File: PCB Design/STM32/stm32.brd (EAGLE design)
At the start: 71.1 x 45.7 mm, 68 parts, among them IC1 NCP1117ST50T3G, Q1 8MHz, T1 SFH303, T2 SFH303, T3 SFH303, T4 SFH303, U1 STM32F103RET6, U2 MCP1700T-3302E/TT, U3 MCP1700T-3302E/TT, U4 MPU-6050, U5 TB6612FNG, X1 22-23-2031

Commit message: update8
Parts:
- moved C15 1.80 mm to (72.1, 34.9)
- moved C19 1.44 mm to (67.6, 34.9), turned to 180 degrees
- moved R9 1.27 mm to (88.9, 72.6), turned to 90 degrees
- moved R8 0.92 mm to (83.8, 72.6), turned to 90 degrees
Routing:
- net 5V: track 61.6 -> 132.7 mm, vias 1 -> 0
- net V_BATT: track 23.4 -> 73.3 mm
- net VCC: track 169.4 -> 135.2 mm
- net IR_OUT3: track 23.5 -> 0.00 mm, vias 2 -> 0
- net USART1_RX: track 14.2 -> 0.00 mm
- net GND: track 183.0 -> 194.6 mm, vias 9 -> 10
- net IR_IN3: track 14.0 -> 23.2 mm
- net IR_IN2: track 0.00 -> 9.24 mm
- net JTAG-TCK: track 6.50 -> 2.64 mm
- net JTAG-TDO: track 11.5 -> 9.16 mm
- net JTAG-TMS: track 9.83 -> 7.67 mm
- net M2-: track 43.4 -> 42.5 mm, vias 1 -> 2
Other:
- outline, holes or cut-outs redrawn

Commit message: meal save
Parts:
- moved U$1 1.02 mm to (97.8, 56.1)
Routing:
- net VCC: track 135.2 -> 67.7 mm
- net M2CB: track 32.7 -> 0.00 mm
- net M2CA: track 26.0 -> 0.00 mm
- net USART1_TX: track 15.5 -> 0.00 mm, vias 1 -> 0
- net GND: track 194.6 -> 179.3 mm, vias 10 -> 15
- net RST: track 14.8 -> 0.00 mm
- net LED3: track 0.00 -> 14.0 mm
- net IR_IN3: track 23.2 -> 9.24 mm, vias 1 -> 0
- net IR_IN4: track 12.8 -> 0.00 mm, vias 1 -> 0
- net N$14: track 0.00 -> 10.2 mm
- net JTAG-TDO: track 9.16 -> 0.06 mm
- net N$7: track 0.00 -> 7.84 mm, vias 0 -> 1
- net JTAG-TMS: track 7.67 -> 0.06 mm
- net N$5: track 0.00 -> 5.85 mm, vias 0 -> 1
- net JTAG-TCK: track 2.64 -> 0.00 mm
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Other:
- board size 71.1 x 45.7 mm -> 71.1 x 81.3 mm

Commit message: first darft
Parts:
- moved R19 8.38 mm to (104.4, 4.06)
- moved JP3 6.48 mm to (73.7, 12.6)
- moved JP4 6.48 mm to (99.1, 12.6)
- moved C14 5.84 mm to (92.5, 4.06)
- moved C8 5.84 mm to (79.2, 4.06)
- moved IC1 5.84 mm to (85.6, 4.06)
- moved S1 5.84 mm to (98.0, 4.32)
- moved X1 5.84 mm to (73.4, 5.08)
- moved R22 3.56 mm to (104.4, 6.35)
- moved LED6 2.30 mm to (102.6, 36.1)
- moved LED7 2.30 mm to (102.6, 37.8)
- moved LED5 2.30 mm to (102.6, 34.3)
- moved R16 2.05 mm to (99.6, 36.1)
- moved R17 2.05 mm to (99.6, 37.8)
- moved R15 2.05 mm to (99.6, 34.3)
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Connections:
- net IR_OUT1: now also U1.40; no longer U1.37
- net IR_OUT2: now also U1.39; no longer U1.38
- net IR_OUT3: now also U1.38; no longer U1.39
- net IR_OUT4: now also U1.37; no longer U1.40
- net M1CA: now also JP4.6; no longer JP3.6
- net M1CB: now also JP4.5; no longer JP3.5
- net M2CA: now also JP3.6, U1.36; no longer JP4.6, U1.35
- net M2CB: now also JP3.5, U1.35; no longer JP4.5, U1.36
- net USART1_RX: now also U$1.6; no longer U$1.4
- net USART1_TX: now also U$1.4; no longer U$1.6
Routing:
- net VCC: track 67.7 -> 175.9 mm, vias 5 -> 10
- net M2CB: track 0.00 -> 75.3 mm, vias 0 -> 1
- net M2CA: track 0.00 -> 75.3 mm, vias 0 -> 1
- net 5V: track 132.7 -> 201.2 mm, vias 0 -> 1
- net IR_OUT2: track 0.00 -> 42.6 mm
- net M1CB: track 0.00 -> 39.0 mm
- net IR_IN3: track 9.24 -> 48.2 mm, vias 0 -> 2
- net M1CA: track 0.00 -> 37.0 mm, vias 0 -> 2
- net GND: track 179.3 -> 216.1 mm, vias 15 -> 20
- net IR_IN1: track 0.00 -> 36.6 mm, vias 0 -> 1
- net IR_IN4: track 0.00 -> 36.5 mm, vias 0 -> 2
- net IR_IN2: track 9.24 -> 45.5 mm, vias 0 -> 2
- net IR_OUT3: track 0.00 -> 34.4 mm
- net IR_OUT1: track 0.00 -> 31.6 mm, vias 0 -> 2
- net RST: track 0.00 -> 28.1 mm, vias 0 -> 2
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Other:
- board size 71.1 x 81.3 mm -> 71.1 x 86.4 mm

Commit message: second draft
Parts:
- moved R19 59.4 mm to (74.4, 55.4), turned to 180 degrees
- moved S1 59.2 mm to (77.2, 59.7), turned to 0 degrees
- moved R22 55.4 mm to (78.5, 55.4)
- moved IC1 1.83 mm to (86.6, 5.59)
- moved C8 1.70 mm to (80.0, 5.59)
- moved C14 1.55 mm to (92.7, 5.59)
- moved X1 1.37 mm to (74.7, 5.59)
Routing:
- net BUTTON1: track 0.00 -> 31.2 mm, vias 0 -> 2
- net GND: track 216.1 -> 231.8 mm
- net 5V: track 201.2 -> 192.8 mm, vias 1 -> 2
- net N$31: track 4.59 -> 7.14 mm
- net VCC: track 175.9 -> 177.9 mm
- net IR_IN1: track 36.6 -> 35.1 mm, vias 1 -> 2
- net V_BATT: track 79.0 -> 77.8 mm
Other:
- board size 71.1 x 86.4 mm -> 71.1 x 84.3 mm

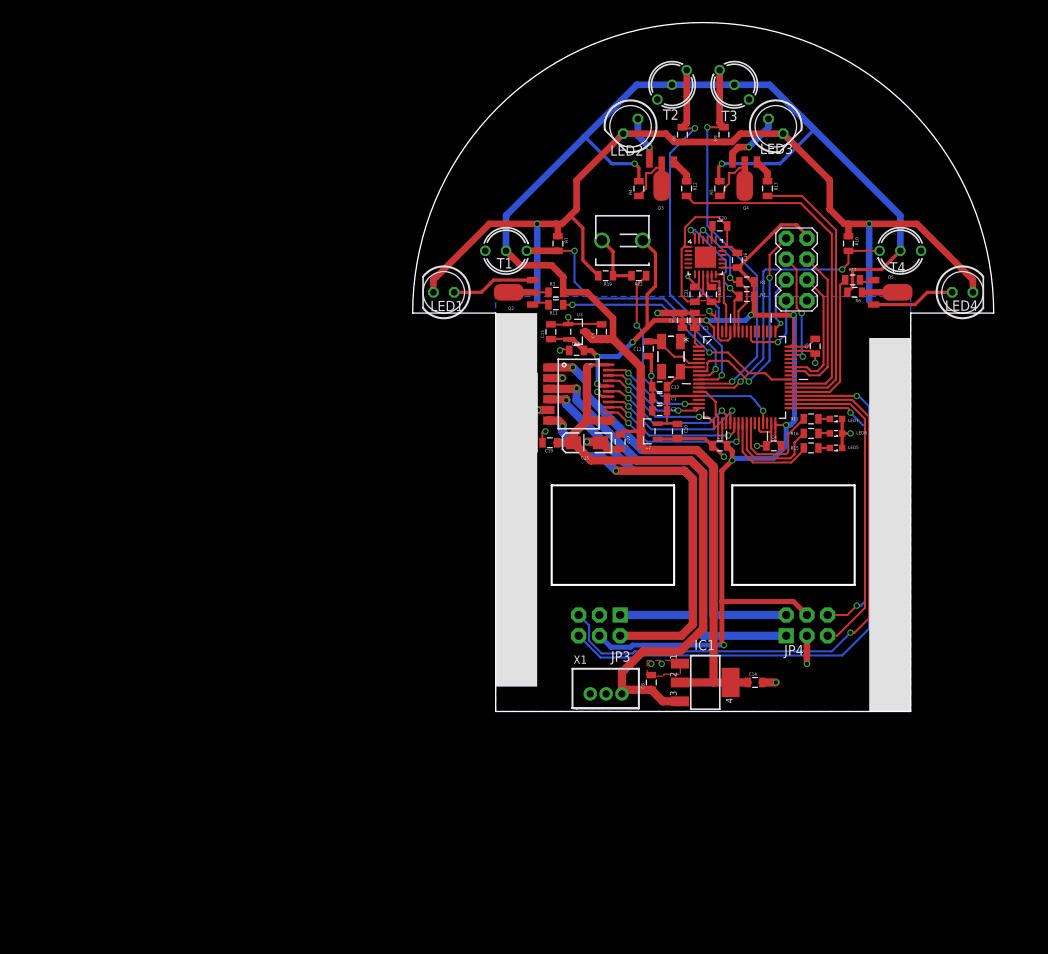
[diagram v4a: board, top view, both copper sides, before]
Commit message: changed the transistor to BC847 with package SOT23
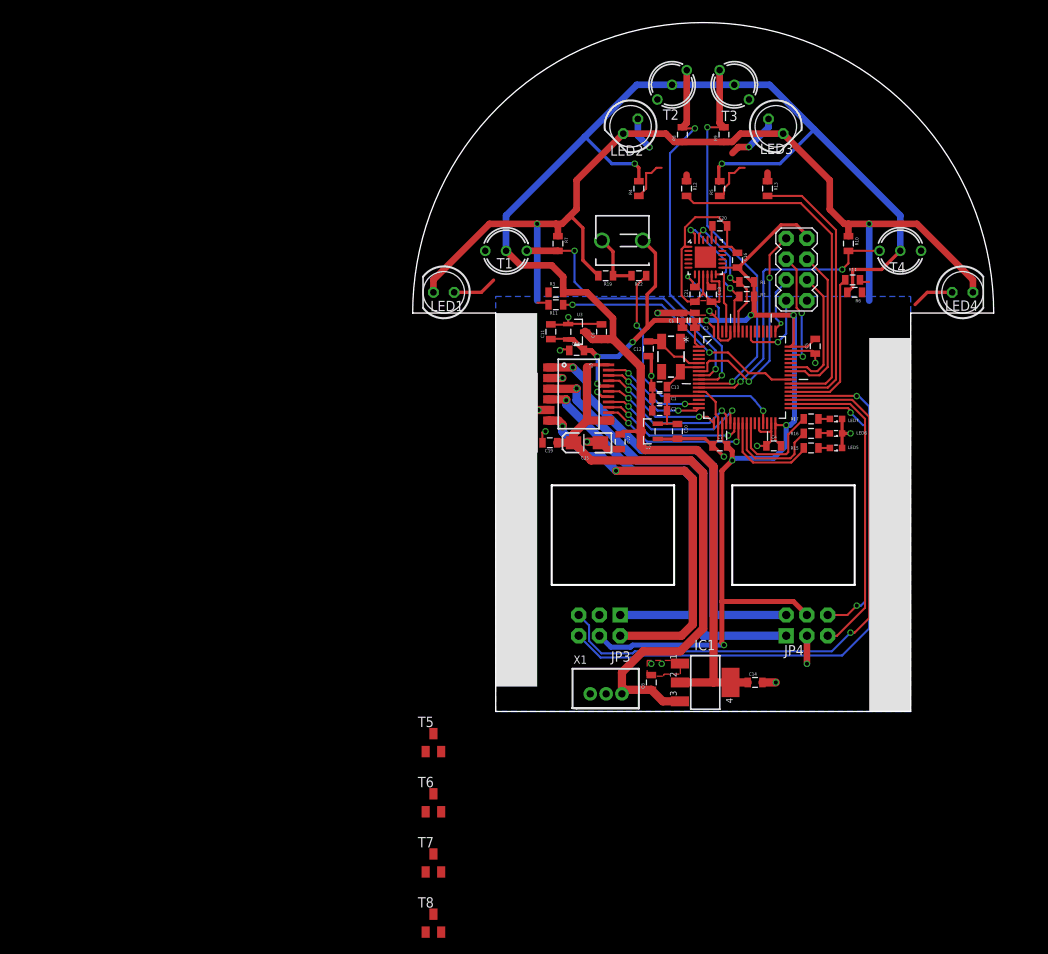
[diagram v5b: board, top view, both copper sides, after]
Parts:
- removed Q2, Q3, Q4, Q5: (no value), semicon-smd-ipc:SOT89
- added T5, T6, T7, T8: BC847, transistor:SOT23
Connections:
- net N$14: now also T8.2; no longer Q5.3
- net N$15: now also T5.3; no longer Q2.2
- net N$16: now also T7.3; no longer Q4.2
- net N$17: now also T8.3; no longer Q5.2
- net N$22: now also T8.1; no longer Q5.1
- net N$23: now also T7.1; no longer Q4.1
- net N$24: now also T6.1; no longer Q3.1
- net N$25: now also T5.1; no longer Q2.1
- net N$3: now also T6.3; no longer Q3.2
- net N$4: now also T5.2; no longer Q2.3
- net N$5: now also T6.2; no longer Q3.3
- net N$7: now also T7.2; no longer Q4.3
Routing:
- net N$14: track 10.2 -> 5.17 mm
- net N$4: track 10.2 -> 5.45 mm
- net N$15: track 2.20 -> 0.00 mm
- net N$24: track 2.99 -> 0.80 mm
- net N$23: track 2.89 -> 1.06 mm
- net N$5: track 5.85 -> 4.05 mm
- net N$17: track 1.69 -> 0.00 mm
- net N$7: track 7.84 -> 6.75 mm
- net N$25: track 2.15 -> 1.55 mm
- net N$22: track 2.16 -> 1.56 mm
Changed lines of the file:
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@@
 <attribute name="VALUE" x="84.963" y="42.926" size="0.4064" layer="27" rot="R90"/>
-</element>
-<element name="Q2" library="semicon-smd-ipc" package="SOT89" value="" x="63.5" y="53.34" locked="yes" smashed="yes" rot="R90">
-<attribute name="NAME" x="62.484" y="51.181" size="0.4064" layer="25"/>
-<attribute name="VALUE" x="67.8449" y="50.9349" size="1.27" layer="27" rot="R90"/>
-</element>
-<element name="Q3" library="semicon-smd-ipc" package="SOT89" value="" x="81.28" y="67.31" locked="yes" smashed="yes" rot="R180">
-<attribute name="NAME" x="81.534" y="63.881" size="0.4064" layer="25" rot="R180"/>
-<attribute name="VALUE" x="83.6851" y="71.6549" size="1.27" layer="27" rot="R180"/>
-</element>
-<element name="Q4" library="semicon-smd-ipc" package="SOT89" value="" x="91.44" y="67.31" locked="yes" smashed="yes" rot="R180">
-<attribute name="NAME" x="91.948" y="63.881" size="0.4064" layer="25" rot="R180"/>
-<attribute name="VALUE" x="93.8451" y="71.6549" size="1.27" layer="27" rot="R180"/>
-</element>
-<element name="Q5" library="semicon-smd-ipc" package="SOT89" value="" x="109.22" y="53.34" locked="yes" smashed="yes" rot="R270">
-<attribute name="NAME" x="108.966" y="54.991" size="0.4064" layer="25"/>
-<attribute name="VALUE" x="104.8751" y="55.7451" size="1.27" layer="27" rot="R270"/>
 </element>
 <element name="R1" library="SparkFun-Passives" package="0805" value="10k" x="91.694" y="54.61" smashed="yes">
@@
 <attribute name="VALUE" x="93.345" y="61.214" size="1.27" layer="27" rot="R270"/>
 </element>
+<element name="T5" library="transistor" package="SOT23" value="BC847" x="53.34" y="-1.778"/>
+<element name="T6" library="transistor" package="SOT23" value="BC847" x="53.34" y="-9.144"/>
+<element name="T7" library="transistor" package="SOT23" value="BC847" x="53.34" y="-16.51"/>
+<element name="T8" library="transistor" package="SOT23" value="BC847" x="53.34" y="-23.876"/>
 </elements>
 <signals>
@@
 </signal>
 <signal name="N$22">
-<contactref element="Q5" pad="1"/>
 <contactref element="R14" pad="1"/>
 <wire x1="106.68" y1="54.61" x2="105.41" y2="54.61" width="0.254" layer="1"/>
 <wire x1="105.41" y1="54.61" x2="105.548" y2="54.864" width="0.254" layer="1"/>
-<wire x1="106.68" y1="54.61" x2="107.239" y2="54.839" width="0.254" layer="1"/>
+<contactref element="T8" pad="1"/>
+<wire x1="52.39" y1="-24.976" x2="105.41" y2="54.61" width="0" layer="19" extent="1-1"/>
 </signal>
 <signal name="N$23">
-<contactref element="Q4" pad="1"/>
 <contactref element="R13" pad="1"/>
-<wire x1="92.939" y1="69.291" x2="94.234" y2="67.996" width="0.8128" layer="1"/>
 <wire x1="94.234" y1="67.996" x2="94.234" y2="66.94" width="0.8128" layer="1"/>
+<contactref element="T7" pad="1"/>
+<wire x1="52.39" y1="-17.61" x2="94.234" y2="66.94" width="0" layer="19" extent="1-1"/>
 </signal>
 <signal name="N$24">
-<contactref element="Q3" pad="1"/>
 <contactref element="R12" pad="1"/>
-<wire x1="82.779" y1="69.291" x2="84.328" y2="67.742" width="0.8128" layer="1"/>
 <wire x1="84.328" y1="67.742" x2="84.328" y2="66.94" width="0.8128" layer="1"/>
+<contactref element="T6" pad="1"/>
+<wire x1="52.39" y1="-10.244" x2="84.328" y2="66.94" width="0" layer="19" extent="1-1"/>
 </signal>
 <signal name="N$25">
-<contactref element="Q2" pad="1"/>
 <contactref element="R11" pad="1"/>
 <wire x1="66.04" y1="52.07" x2="67.31" y2="52.07" width="0.254" layer="1"/>
 <wire x1="67.31" y1="52.07" x2="67.426" y2="51.816" width="0.254" layer="1"/>
-<wire x1="66.04" y1="52.07" x2="65.481" y2="51.841" width="0.254" layer="1"/>
+<contactref element="T5" pad="1"/>
+<wire x1="52.39" y1="-2.878" x2="66.04" y2="52.07" width="0" layer="19" extent="1-1"/>
 </signal>
 <signal name="N$26">
@@
 </signal>
 <signal name="N$3">
-<contactref element="Q3" pad="2"/>
 <contactref element="R4" pad="1"/>
 <wire x1="79.375" y1="66.04" x2="78.74" y2="65.405" width="0.254" layer="1"/>
@@
 <wire x1="81.28" y1="68.58" x2="80.645" y2="68.58" width="0.254" layer="1"/>
 <wire x1="78.74" y1="65.405" x2="78.486" y2="65.14" width="0.254" layer="1"/>
-<wire x1="81.28" y1="68.58" x2="81.28" y2="69.037" width="0.254" layer="1"/>
+<contactref element="T6" pad="3"/>
+<wire x1="53.34" y1="-8.044" x2="78.486" y2="65.14" width="0" layer="19" extent="1-1"/>
 </signal>
 <signal name="N$4">
-<contactref element="Q2" pad="3"/>
 <contactref element="LED1" pad="A"/>
-<wire x1="60.706" y1="54.839" x2="65.481" y2="54.839" width="0.4064" layer="1"/>
 <wire x1="55.88" y1="53.34" x2="59.207" y2="53.34" width="0.4064" layer="1"/>
 <wire x1="59.207" y1="53.34" x2="60.706" y2="54.839" width="0.4064" layer="1"/>
+<contactref element="T5" pad="2"/>
+<wire x1="54.29" y1="-2.878" x2="55.88" y2="53.34" width="0" layer="19" extent="1-1"/>
 </signal>
 <signal name="N$5">
-<contactref element="Q3" pad="3"/>
 <contactref element="LED2" pad="A"/>
 <wire x1="78.368025" y1="74.558025" x2="78.368025" y2="72.507975" width="0.8128" layer="16"/>
-<wire x1="79.781" y1="69.291" x2="79.781" y2="71.095" width="0.8128" layer="1"/>
 <via x="79.781" y="71.095" extent="1-16" drill="0.5"/>
 <wire x1="79.781" y1="71.095" x2="78.368025" y2="72.507975" width="0.8128" layer="16"/>
+<contactref element="T6" pad="2"/>
+<wire x1="54.29" y1="-10.244" x2="79.781" y2="71.095" width="0" layer="19" extent="1-1"/>
 </signal>
 <signal name="N$7">
-<contactref element="Q4" pad="3"/>
 <contactref element="LED3" pad="A"/>
 <wire x1="94.351971875" y1="74.558025" x2="94.351971875" y2="73.523971875" width="0.8128" layer="16"/>
@@
 <via x="91.948" y="71.12" extent="1-16" drill="0.5"/>
 <wire x1="91.948" y1="71.12" x2="90.678" y2="71.12" width="0.8128" layer="1"/>
-<wire x1="89.941" y1="69.291" x2="89.941" y2="70.383" width="0.8128" layer="1"/>
 <wire x1="89.941" y1="70.383" x2="90.678" y2="71.12" width="0.8128" layer="1"/>
+<contactref element="T7" pad="2"/>
+<wire x1="54.29" y1="-17.61" x2="89.941" y2="70.383" width="0" layer="19" extent="1-1"/>
 </signal>
 <signal name="N$14">
-<contactref element="Q5" pad="3"/>
 <contactref element="LED4" pad="A"/>
 <wire x1="116.84" y1="53.34" x2="113.792" y2="53.34" width="0.4064" layer="1"/>
-<wire x1="107.239" y1="51.841" x2="112.293" y2="51.841" width="0.4064" layer="1"/>
 <wire x1="112.293" y1="51.841" x2="113.792" y2="53.34" width="0.4064" layer="1"/>
+<contactref element="T8" pad="2"/>
+<wire x1="54.29" y1="-24.976" x2="112.293" y2="51.841" width="0" layer="19" extent="1-1"/>
 </signal>
 <signal name="N$15">
 <contactref element="R3" pad="1"/>
-<contactref element="Q2" pad="2"/>
-<wire x1="65.227" y1="53.34" x2="67.426" y2="53.34" width="0.254" layer="1"/>
+<contactref element="T5" pad="3"/>
+<wire x1="53.34" y1="-0.678" x2="67.426" y2="53.34" width="0" layer="19" extent="1-1"/>
 </signal>
 <signal name="N$16">
 <contactref element="R5" pad="1"/>
-<contactref element="Q4" pad="2"/>
 <wire x1="88.9" y1="66.04" x2="88.9" y2="65.405" width="0.254" layer="1"/>
 <wire x1="89.535" y1="66.675" x2="88.9" y2="66.04" width="0.254" layer="1"/>
@@
 <wire x1="91.44" y1="68.58" x2="90.805" y2="68.58" width="0.254" layer="1"/>
 <wire x1="88.9" y1="65.405" x2="88.392" y2="65.14" width="0.254" layer="1"/>
-<wire x1="91.44" y1="68.58" x2="91.44" y2="69.037" width="0.254" layer="1"/>
+<contactref element="T7" pad="3"/>
+<wire x1="53.34" y1="-15.41" x2="88.392" y2="65.14" width="0" layer="19" extent="1-1"/>
 </signal>
 <signal name="N$17">
 <contactref element="R6" pad="1"/>
-<contactref element="Q5" pad="2"/>
-<wire x1="107.493" y1="53.34" x2="105.802" y2="53.34" width="0.6096" layer="1"/>
+<contactref element="T8" pad="3"/>
+<wire x1="53.34" y1="-22.776" x2="105.802" y2="53.34" width="0" layer="19" extent="1-1"/>
 </signal>
 </signals>

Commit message: update according to the change
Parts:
- moved T8 95.6 mm to (109.7, 53.3), turned to 90 degrees
- moved T7 91.6 mm to (91.4, 66.8), turned to 180 degrees
- moved T6 80.9 mm to (81.3, 66.8), turned to 180 degrees
- moved T5 56.0 mm to (63.0, 53.3), turned to 90 degrees
- moved R14 3.06 mm to (104.9, 51.8)
- moved R11 0.51 mm to (67.8, 51.8)
- moved R3 0.51 mm to (67.8, 53.3)
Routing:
- net N$15: track 0.00 -> 5.03 mm
- net N$4: track 5.45 -> 9.29 mm
- net N$22: track 1.56 -> 5.26 mm
- net N$5: track 4.05 -> 7.47 mm
- net IR_OUT4: track 19.3 -> 16.4 mm
- net N$17: track 0.00 -> 2.83 mm
- net N$3: track 5.34 -> 3.03 mm
- net N$16: track 5.54 -> 3.28 mm
- net 5V: track 192.8 -> 191.0 mm
- net N$24: track 0.80 -> 2.50 mm
- net N$25: track 1.55 -> 3.06 mm
- net N$7: track 6.75 -> 8.26 mm
- net N$14: track 5.17 -> 6.41 mm
- net N$23: track 1.06 -> 2.24 mm
- net IR_OUT1: track 31.6 -> 32.1 mm

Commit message: third draft
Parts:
- C12, C13: value 33pF -> 10pF
- Q1: value 8MHz -> ABM3B-8.000MHZ-10-1UT; device SparkFun2:CRYSTAL-SMD-5X3 -> SparkFun-FreqCtrl:CRYSTAL-SMD-5X3
- moved C2 48.5 mm to (32.5, 39.8)
- moved C10 48.5 mm to (34.7, 37.1)
- moved C8 48.5 mm to (31.5, 6.35)
- moved C16 48.5 mm to (42.0, 58.0)
- moved C18 48.5 mm to (38.9, 53.8)
- moved C22 48.5 mm to (27.7, 35.8)
- moved C9 48.5 mm to (25.4, 49.3)
- moved IC1 48.5 mm to (38.1, 6.35)
- moved JP4 48.5 mm to (50.5, 13.3)
- moved LED3 48.5 mm to (46.7, 74.4)
- moved LED5 48.5 mm to (54.1, 35.1)
- moved LED6 48.5 mm to (54.1, 36.8)
- moved LED7 48.5 mm to (54.1, 38.6)
- moved Q1 48.5 mm to (33.9, 46.2)
- moved R1 48.5 mm to (43.2, 55.4)
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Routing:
- net GND: track 231.8 -> 231.2 mm
- net M1CA: vias 2 -> 1
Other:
- outline, holes or cut-outs redrawn

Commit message: minor update
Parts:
- moved R8 1.14 mm to (35.8, 74.4)
- moved R9 1.14 mm to (39.9, 74.4)
- moved C18 0.25 mm to (38.6, 53.8)
- moved U4 0.25 mm to (37.8, 58.4)
- moved C16 0.25 mm to (41.8, 58.0)
- moved C20 0.25 mm to (39.6, 62.2)
- moved C21 0.25 mm to (36.6, 53.8)
- moved R1 0.25 mm to (42.9, 55.4)
- moved R2 0.25 mm to (42.9, 53.6)
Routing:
- net IR_IN2: track 46.0 -> 44.6 mm
- net IR_IN3: track 48.4 -> 47.2 mm
- net GND: track 231.2 -> 230.1 mm
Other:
- outline, holes or cut-outs redrawn
